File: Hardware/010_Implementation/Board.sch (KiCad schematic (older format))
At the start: 0 parts

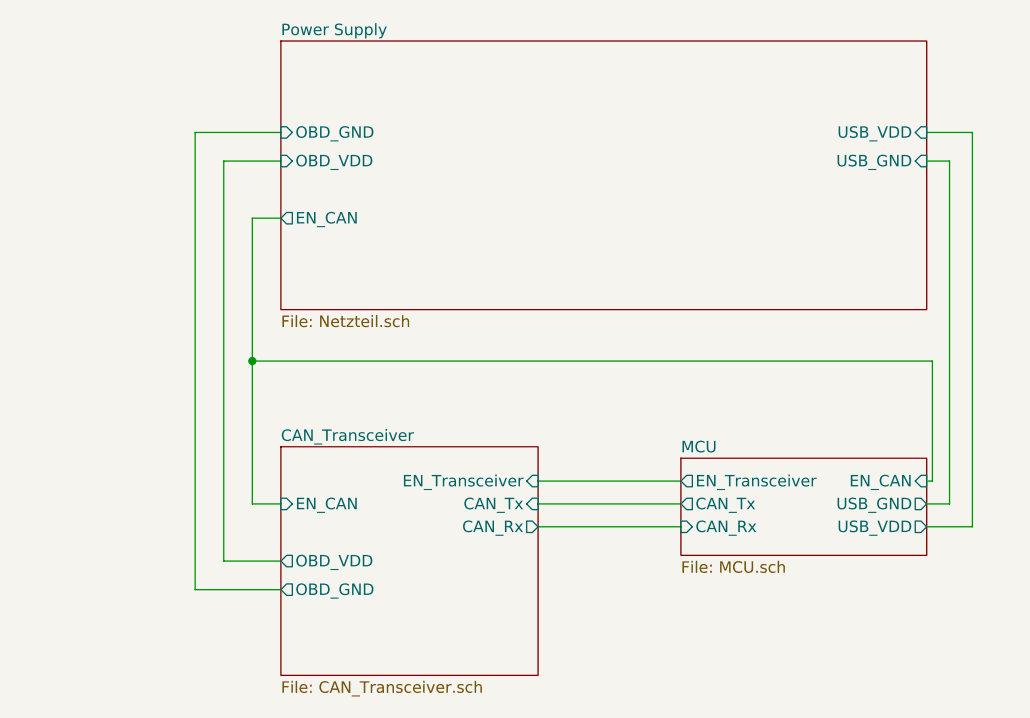
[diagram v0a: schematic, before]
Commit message: Modified Board Schematic. Optimized supply and switching system through Software
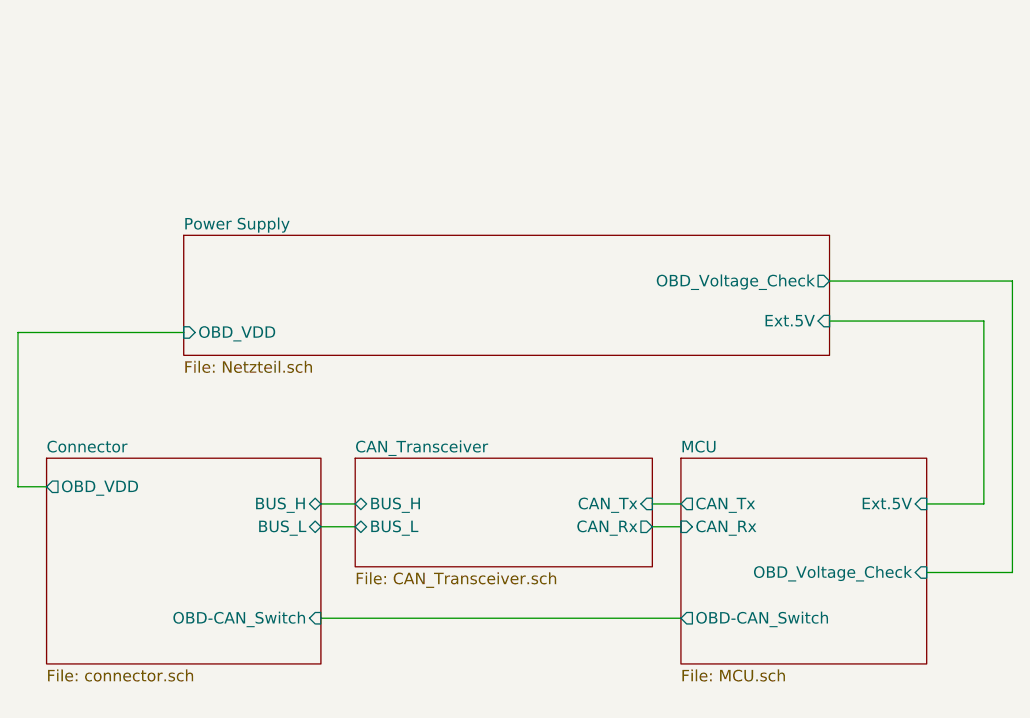
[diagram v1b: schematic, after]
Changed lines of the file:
@@
 $Descr A4 11693 8268
 encoding utf-8
-Sheet 1 7
+Sheet 1 5
 Title "CAN_Bus Analyzer"
 Date "2020-09-07"
@@
 $EndDescr
 $Sheet
-S 4325 1800 2825 1175
+S 3900 2650 2825 525
 U 5F52EFB7
 F0 "Power Supply" 50
 F1 "Netzteil.sch" 50
-F2 "EN_CAN" O L 4325 2575 50
-F3 "OBD_VDD" I L 4325 2325 50
-F4 "OBD_GND" I L 4325 2200 50
-F5 "USB_VDD" I R 7150 2200 50
-F6 "USB_GND" I R 7150 2325 50
+F2 "OBD_VDD" I L 3900 3075 50
+F3 "Ext.5V" I R 6725 3025 50
+F4 "OBD_Voltage_Check" O R 6725 2850 50
 $EndSheet
 $Sheet
-S 4325 3575 1125 1000
+S 4650 3625 1300 475
 U 5F562A6B
 F0 "CAN_Transceiver" 50
 F1 "CAN_Transceiver.sch" 50
-F2 "CAN_Rx" O R 5450 3925 50
-F3 "CAN_Tx" I R 5450 3825 50
-F4 "OBD_VDD" O L 4325 4075 50
-F5 "OBD_GND" O L 4325 4200 50
-F6 "EN_CAN" I L 4325 3825 50
-F7 "EN_Transceiver" I R 5450 3725 50
+F2 "CAN_Rx" O R 5950 3925 50
+F3 "CAN_Tx" I R 5950 3825 50
+F4 "BUS_H" B L 4650 3825 50
+F5 "BUS_L" B L 4650 3925 50
 $EndSheet
-Wire Wire Line
-	5450 3825 6075 3825
-Wire Wire Line
-	6075 3925 5450 3925
-Wire Wire Line
-	4325 2575 4200 2575
-Wire Wire Line
-	4200 2575 4200 3200
-Wire Wire Line
-	4200 3825 4325 3825
-Wire Wire Line
-	4325 4075 4075 4075
-Wire Wire Line
-	4075 4075 4075 2325
-Wire Wire Line
-	4075 2325 4325 2325
-Wire Wire Line
-	4325 2200 3950 2200
-Wire Wire Line
-	3950 2200 3950 4200
-Wire Wire Line
-	3950 4200 4325 4200
 $Sheet
-S 6075 3625 1075 425
+S 6075 3625 1075 900
 U 5F52F099
 F0 "MCU" 50
@@
 F2 "CAN_Tx" O L 6075 3825 50
 F3 "CAN_Rx" I L 6075 3925 50
-F4 "USB_GND" O R 7150 3825 50
-F5 "USB_VDD" O R 7150 3925 50
-F6 "EN_Transceiver" O L 6075 3725 50
-F7 "EN_CAN" I R 7150 3725 50
+F4 "Ext.5V" I R 7150 3825 50
+F5 "OBD_Voltage_Check" I R 7150 4125 50
+F6 "OBD-CAN_Switch" O L 6075 4325 50
 $EndSheet
 Wire Wire Line
-	7150 3825 7250 3825
+	7150 3825 7400 3825
+$Sheet
+S 3300 3625 1200 900
+U 5FA55ABF
+F0 "Connector" 50
+F1 "connector.sch" 50
+F2 "OBD_VDD" O L 3300 3750 50
+F3 "BUS_H" B R 4500 3825 50
+F4 "BUS_L" B R 4500 3925 50
+F5 "OBD-CAN_Switch" I R 4500 4325 50
+$EndSheet
 Wire Wire Line
-	7250 3825 7250 2325
+	5950 3825 6075 3825
 Wire Wire Line
-	7250 2325 7150 2325
+	6075 3925 5950 3925
 Wire Wire Line
-	7150 2200 7350 2200
+	4500 3825 4650 3825
 Wire Wire Line
-	7350 2200 7350 3925
+	4650 3925 4500 3925
 Wire Wire Line
-	7350 3925 7150 3925
+	6725 3025 7400 3025
 Wire Wire Line
-	5450 3725 6075 3725
+	7400 3025 7400 3825
 Wire Wire Line
-	7150 3725 7175 3725
+	3300 3750 3175 3750
 Wire Wire Line
-	7175 3725 7175 3200
+	3175 3750 3175 3075
 Wire Wire Line
-	7175 3200 4200 3200
-Connection ~ 4200 3200
+	3175 3075 3900 3075
 Wire Wire Line
-	4200 3200 4200 3825
+	4500 4325 6075 4325
+Wire Wire Line
+	6725 2850 7525 2850
+Wire Wire Line
+	7525 2850 7525 4125
+Wire Wire Line
+	7525 4125 7150 4125
 $EndSCHEMATC

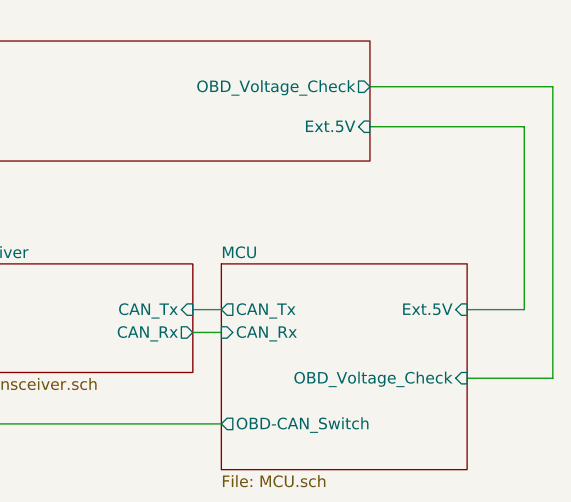
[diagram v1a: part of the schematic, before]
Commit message: Added Missing 5V marker
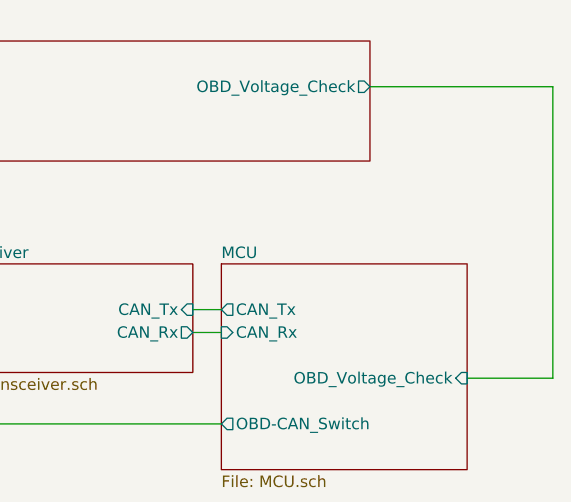
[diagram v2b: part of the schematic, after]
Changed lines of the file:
@@
 F1 "Netzteil.sch" 50
 F2 "OBD_VDD" I L 3900 3075 50
-F3 "Ext.5V" I R 6725 3025 50
-F4 "OBD_Voltage_Check" O R 6725 2850 50
+F3 "OBD_Voltage_Check" O R 6725 2850 50
 $EndSheet
 $Sheet
@@
 F2 "CAN_Tx" O L 6075 3825 50
 F3 "CAN_Rx" I L 6075 3925 50
-F4 "Ext.5V" I R 7150 3825 50
-F5 "OBD_Voltage_Check" I R 7150 4125 50
-F6 "OBD-CAN_Switch" O L 6075 4325 50
+F4 "OBD_Voltage_Check" I R 7150 4125 50
+F5 "OBD-CAN_Switch" O L 6075 4325 50
 $EndSheet
-Wire Wire Line
-	7150 3825 7400 3825
 $Sheet
 S 3300 3625 1200 900
@@
 	4650 3925 4500 3925
 Wire Wire Line
-	6725 3025 7400 3025
-Wire Wire Line
-	7400 3025 7400 3825
-Wire Wire Line
 	3300 3750 3175 3750

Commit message: Board Version 5
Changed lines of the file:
@@
 F3 "CAN_Rx" I L 6075 3925 50
 F4 "OBD_Voltage_Check" I R 7150 4125 50
-F5 "OBD-CAN_Switch" O L 6075 4325 50
+F5 "~OBD~\\CAN" O L 6075 4325 50
 $EndSheet
 $Sheet
@@
 F3 "BUS_H" B R 4500 3825 50
 F4 "BUS_L" B R 4500 3925 50
-F5 "OBD-CAN_Switch" I R 4500 4325 50
+F5 "~OBD~\\CAN" I R 4500 4325 50
 $EndSheet
 Wire Wire Line

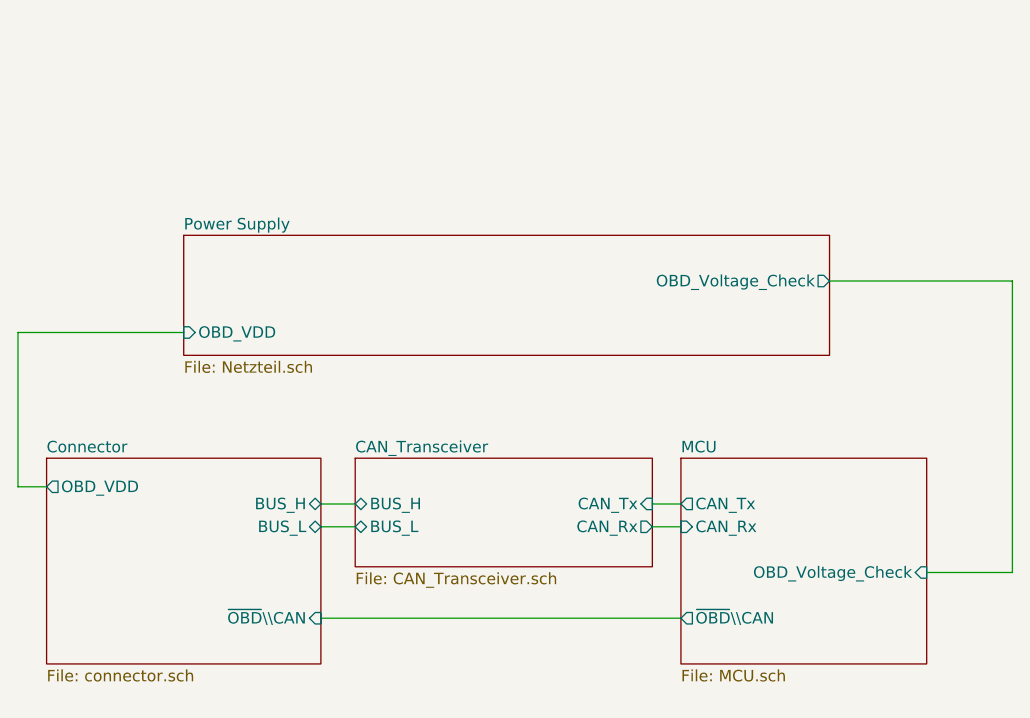
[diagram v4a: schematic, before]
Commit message: Board Version 1.1 Fixed Relay Supply, standard Pins for CAN Transceiver and added CAN high and Low Labels
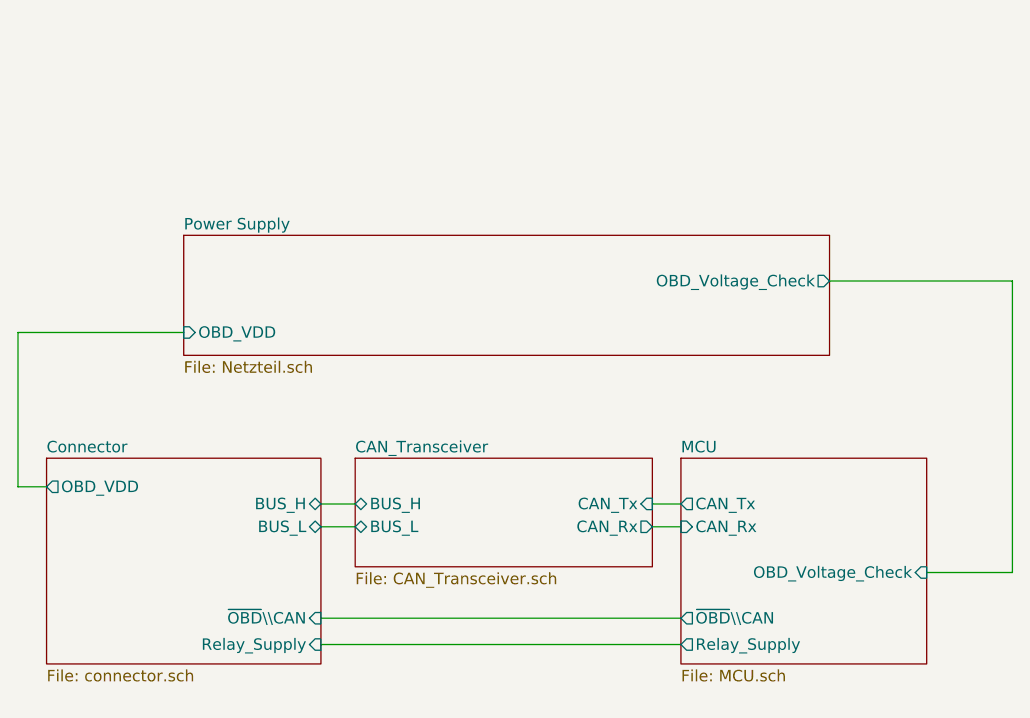
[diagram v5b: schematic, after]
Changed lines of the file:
@@
 F4 "OBD_Voltage_Check" I R 7150 4125 50
 F5 "~OBD~\\CAN" O L 6075 4325 50
+F6 "Relay_Supply" O L 6075 4440 50
 $EndSheet
 $Sheet
@@
 F4 "BUS_L" B R 4500 3925 50
 F5 "~OBD~\\CAN" I R 4500 4325 50
+F6 "Relay_Supply" I R 4500 4440 50
 $EndSheet
 Wire Wire Line
@@
 F3 "OBD_Voltage_Check" O R 6725 2850 50
 $EndSheet
+Wire Wire Line
+	4500 4440 6075 4440
 $EndSCHEMATC
